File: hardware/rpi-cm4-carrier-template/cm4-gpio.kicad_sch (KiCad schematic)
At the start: 10 parts, among them J1 USB4110-GF-A_REVB, U1 NLV17SZ07DFT2G

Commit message: Completed PCB Layout
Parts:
- Module1: footprint CM4IO:Raspberry-Pi-4-Compute-Module -> CM4IO:MUnitA
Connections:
- net nLED_Activity: now also Module1.21 (PI_nLED_Activity)
- net nPWR_LED: now also Module1.95 (nPI_LED_PWR)
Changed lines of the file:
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@@
+    (stroke (width 0) (type solid) (color 0 0 0 0))
+  )
+  (wire (pts (xy 104.14 71.12) (xy 119.38 71.12))
     (stroke (width 0) (type solid) (color 0 0 0 0))
   )
@@
     (stroke (width 0) (type solid) (color 0 0 0 0))
   )
+  (wire (pts (xy 104.14 165.1) (xy 116.84 165.1))
+    (stroke (width 0) (type solid) (color 0 0 0 0))
+  )
   (wire (pts (xy 105.41 142.24) (xy 109.22 142.24))
     (stroke (width 0) (type solid) (color 0 0 0 0))
@@
   (wire (pts (xy 266.7 68.58) (xy 254 68.58))
     (stroke (width 0) (type solid) (color 0 0 0 0))
+  )
+  (label "nPWR_LED" (at 116.84 165.1 180)
+    (effects (font (size 1.27 1.27)) (justify right bottom))
+  )
+  (label "nLED_Activity" (at 119.38 71.12 180)
+    (effects (font (size 1.27 1.27)) (justify right bottom))
   )
   (label "nLED_Activity" (at 149.86 72.39 0)
@@
     (property "Reference" "Module1" (id 0) (at 73.66 33.02 0))
     (property "Value" "ComputeModule4-CM4" (id 1) (at 73.66 35.56 0))
-    (property "Footprint" "CM4IO:Raspberry-Pi-4-Compute-Module" (id 2) (at 218.44 128.27 0)
-      (effects (font (size 1.27 1.27)) hide)
-    )
+    (property "Footprint" "CM4IO:MUnitA" (id 2) (at 218.44 128.27 0)
+      (effects (font (size 1.27 1.27)) hide)
+    )

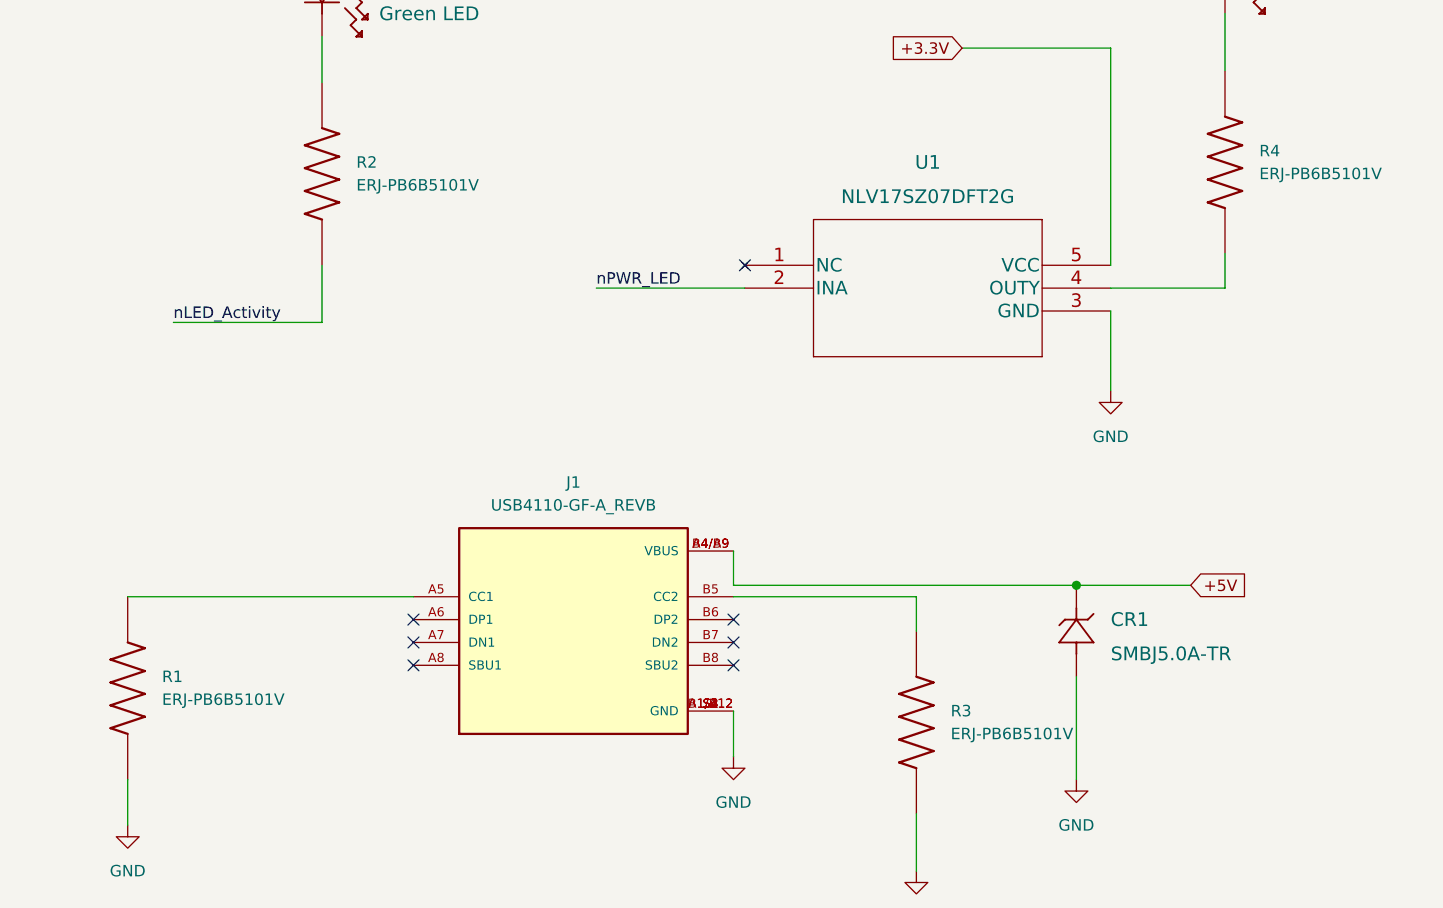
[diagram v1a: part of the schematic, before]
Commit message: updated PCB layout
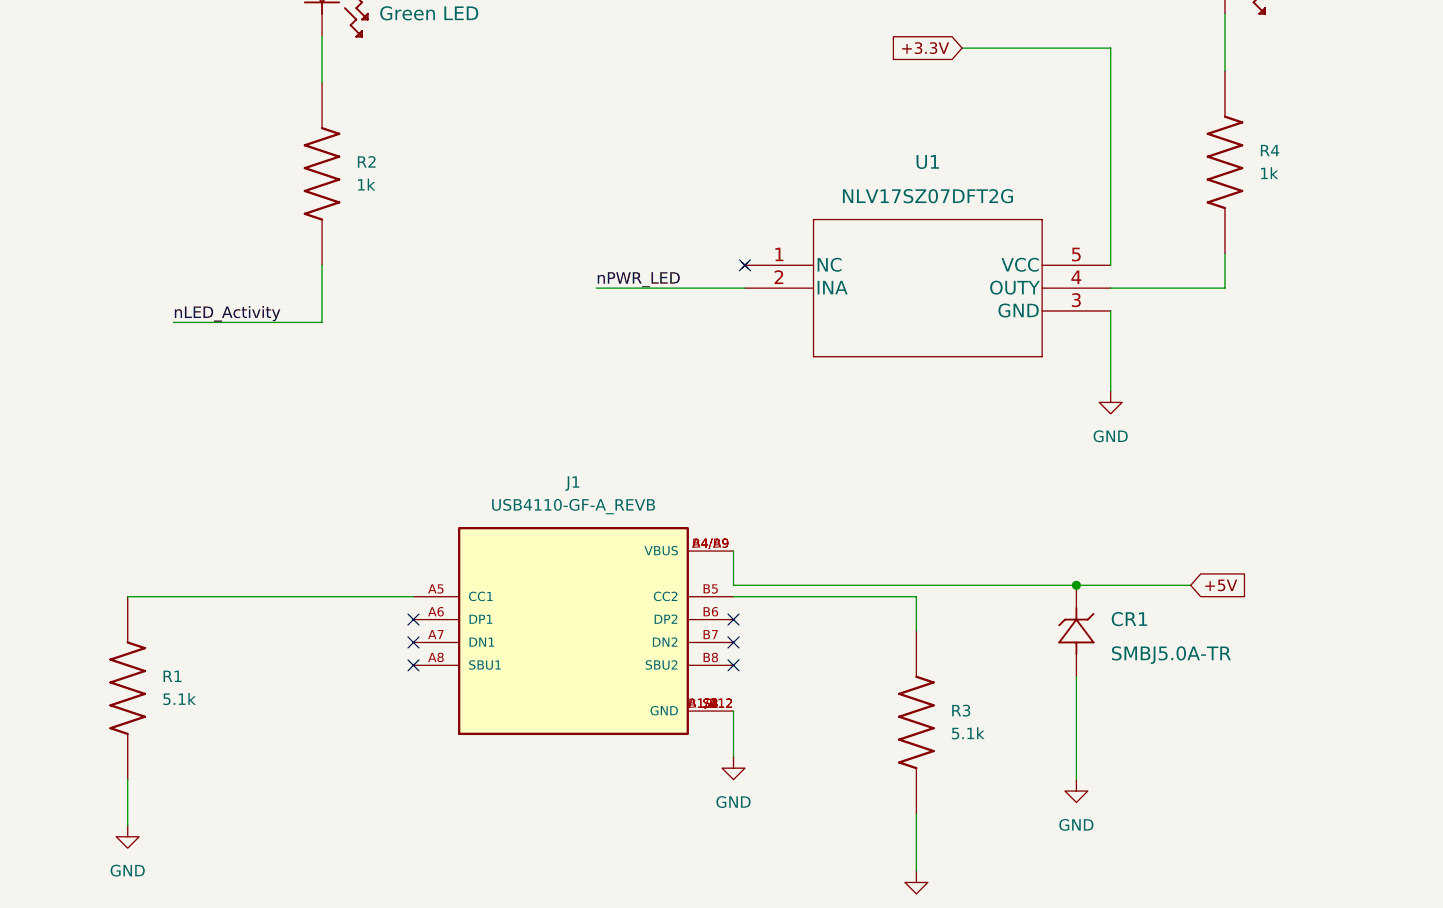
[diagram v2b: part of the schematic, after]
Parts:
- CR1: Digi-Key_PN (none) -> 478-7070-1-ND; Manufacturer (none) -> KYOCERA AVX
- J1: Digi-Key_PN (none) -> 2073-USB4110-GF-A-1-ND; Manufacturer (none) -> GCT
- LED1: Digi-Key_PN (none) -> 754-1057-1-ND; Manufacturer (none) -> Kingbright
- LED2: Digi-Key_PN (none) -> 754-1060-1-ND; Manufacturer (none) -> Kingbright
- Module1: Digi-Key_PN 2x H11615CT-ND -> DF40C-100DS-0.4V(58)-ND; Digi-Key_PN (Alt) 2x H124602CT-ND -> (none)
- R1, R3: value ERJ-PB6B5101V -> 5.1k; Digi-Key_PN (none) -> P20674CT-ND; Manufacturer (none) -> Panasonic Electronic Components
- R2, R4: value ERJ-PB6B5101V -> 1k; Digi-Key_PN (none) -> P20594CT-ND; Manufacturer (none) -> Panasonic Electronic Components
- U1: Digi-Key_PN (none) -> NLV17SZ07DFT2GOSCT-ND; Manufacturer (none) -> onsemi
